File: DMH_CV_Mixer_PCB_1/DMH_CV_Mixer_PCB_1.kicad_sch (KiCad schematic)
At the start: 0 parts

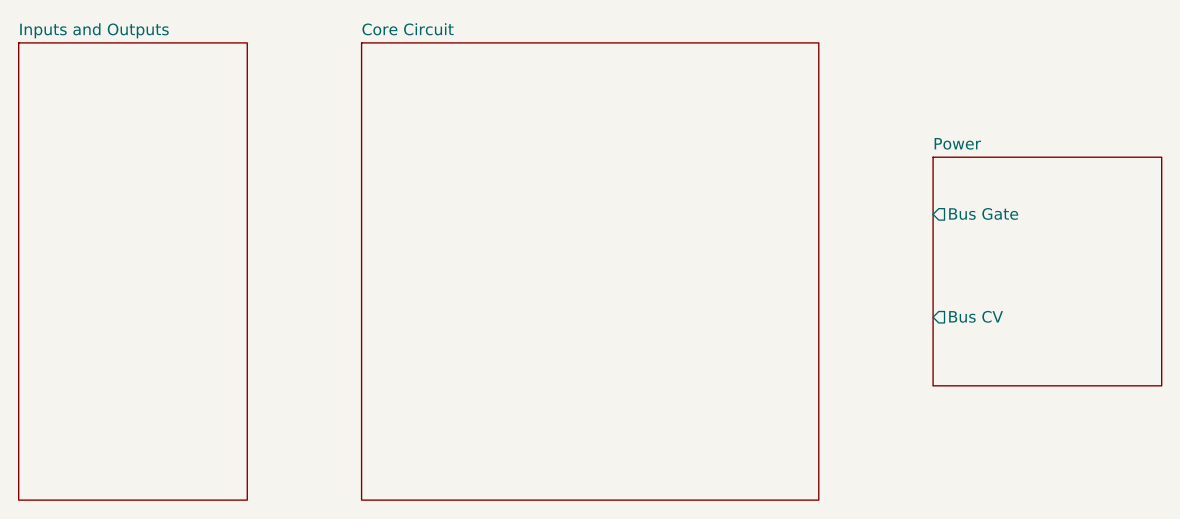
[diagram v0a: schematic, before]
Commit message: Started IO part design
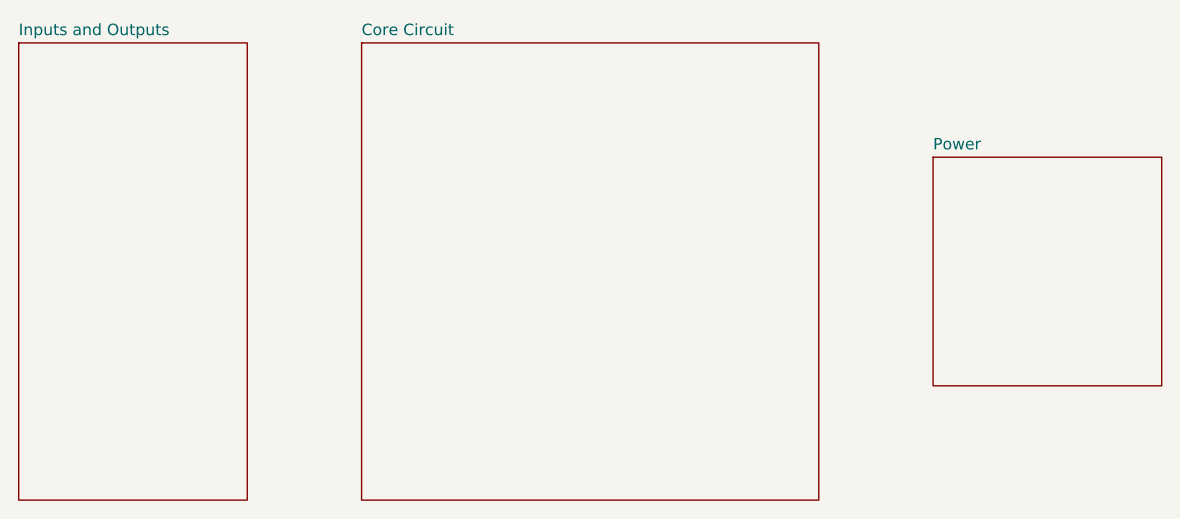
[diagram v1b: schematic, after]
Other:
- sheet Power ports: added none; removed Bus CV, Bus Gate
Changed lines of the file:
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@@
-			)
-		)
-		(pin "Bus Gate" output
-			(at 127 95.25 180)
-			(effects
-				(font
-					(size 1.27 1.27)
-				)
-				(justify left)
-			)
-		)
-		(pin "Bus CV" output
-			(at 127 106.68 180)
-			(effects
-				(font
-					(size 1.27 1.27)
-				)
-				(justify left)
 			)
 		)
 		(instances
-			(project "DMH-Kosmo-5cm-PCB"
+			(project "DMH_CV_Mixer_PCB_1"
 				(path "/58f4306d-5387-4983-bb08-41a2313fd315"
 					(page "4")
@@
 		)
 		(instances
-			(project "DMH-Kosmo-5cm-PCB"
+			(project "DMH_CV_Mixer_PCB_1"
 				(path "/58f4306d-5387-4983-bb08-41a2313fd315"
 					(page "3")
@@
 		)
 		(instances
-			(project "DMH-Kosmo-5cm-PCB"
+			(project "DMH_CV_Mixer_PCB_1"
 				(path "/58f4306d-5387-4983-bb08-41a2313fd315"
 					(page "2")
